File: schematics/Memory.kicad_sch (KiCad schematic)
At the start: 31 parts, among them SW1 SW_DIP_x08, U1 AS6C4008-55PCN, U2 74LS245, U3 74LS157, U4 74LS157, U5 74LS245, U6 74LS04, U7 74LS08

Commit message: chore: full part list & memory module rework
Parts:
- removed C2, C6: 0.1uF, symbol Device:C
- removed U4: 74LS157, symbol 74xx:74LS157
- removed U6: 74LS04, symbol 74xx:74LS04
- removed U7: 74LS08, symbol 74xx:74LS08
- added R9: 10K, symbol Device:R
- added SW2: SW_Push, symbol Switch:SW_Push
- added U4: 74LS00, symbol 74xx:74LS00
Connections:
- net +5V: now also U3.2 (I0a), U3.5 (I0b), R9.1, U4.14 (VCC)
- net BUS_0: now also U2.18 (B0); no longer U2.2 (A0), U5.9 (A7)
- net BUS_1: now also U2.17 (B1); no longer U2.3 (A1), U5.8 (A6)
- net BUS_2: now also U2.16 (B2); no longer U2.4 (A2), U5.7 (A5)
- net BUS_3: now also U2.15 (B3); no longer U2.5 (A3), U5.6 (A4)
- net BUS_4: now also U2.14 (B4); no longer U2.6 (A4), U5.5 (A3)
- net BUS_5: now also U2.13 (B5); no longer U2.7 (A5), U5.4 (A2)
- net BUS_6: now also U2.12 (B6); no longer U2.8 (A6), U5.3 (A1)
- net BUS_7: now also U2.11 (B7); no longer U2.9 (A7), U5.2 (A0)
- net GND: now also U5.1 (A->B), SW2.1, U4.7 (GND)
- net at D1.2 (A), U1.21 (DQ7): now also U2.9 (A7), U5.2 (A0); no longer U2.11 (B7), U3.4 (Za)
- net at D4.2 (A), U1.18 (DQ4): now also U2.6 (A4), U5.5 (A3); no longer U2.14 (B4), U3.12 (Zd)
- net at U2.1 (A->B): now also U1.29 (WE#), U3.6 (I1b), U3.9 (Zc), U4.10; no longer U5.1 (A->B)
- net at D2.2 (A), U1.20 (DQ6): now also U2.8 (A6), U5.3 (A1); no longer U2.12 (B6), U3.7 (Zb)
- net at D3.2 (A), U1.19 (DQ5): now also U2.7 (A5), U5.4 (A2); no longer U2.13 (B5), U3.9 (Zc)
- net at D5.2 (A), U1.17 (DQ3): now also U2.5 (A3), U5.6 (A4); no longer U2.15 (B3)
- net at D6.2 (A), U1.15 (DQ2): now also U2.4 (A2), U5.7 (A5); no longer U2.16 (B2)
- net at D7.2 (A), U1.14 (DQ1): now also U2.3 (A1), U5.8 (A6); no longer U2.17 (B1)
- net at D8.2 (A), U1.13 (DQ0): now also U2.2 (A0), U5.9 (A7); no longer U2.18 (B0)
- net at U2.19 (CE): now also U3.4 (Za)
- net at U5.19 (CE): now also U3.7 (Zb)
- net at SW1.10: now also U5.17 (B1)
- net at SW1.11: now also U5.16 (B2)
- net at SW1.12: now also U5.15 (B3)
- net at SW1.13: now also U5.14 (B4); no longer U3.13 (I1d)
- net at SW1.14: now also U5.13 (B5); no longer U3.10 (I1c)
- net at SW1.15: now also U5.12 (B6); no longer U3.6 (I1b)
- net at U3.3 (I1a): now also U4.6; no longer SW1.16
- net at SW1.9: now also U5.18 (B0)
- net at U3.11 (I0c): now also R9.2, SW2.2; no longer U5.16 (B2)
- net at U3.14 (I0d): no longer U5.15 (B3)
- net at U5.11 (B7): now also SW1.16
- new net: U4.4, U4.5, U4.8
- new net: U3.10 (I1c), U4.3
- new net CLK: U4.2
- new net RAM_IN: U4.1
- new net |RAM_OUT: U4.9

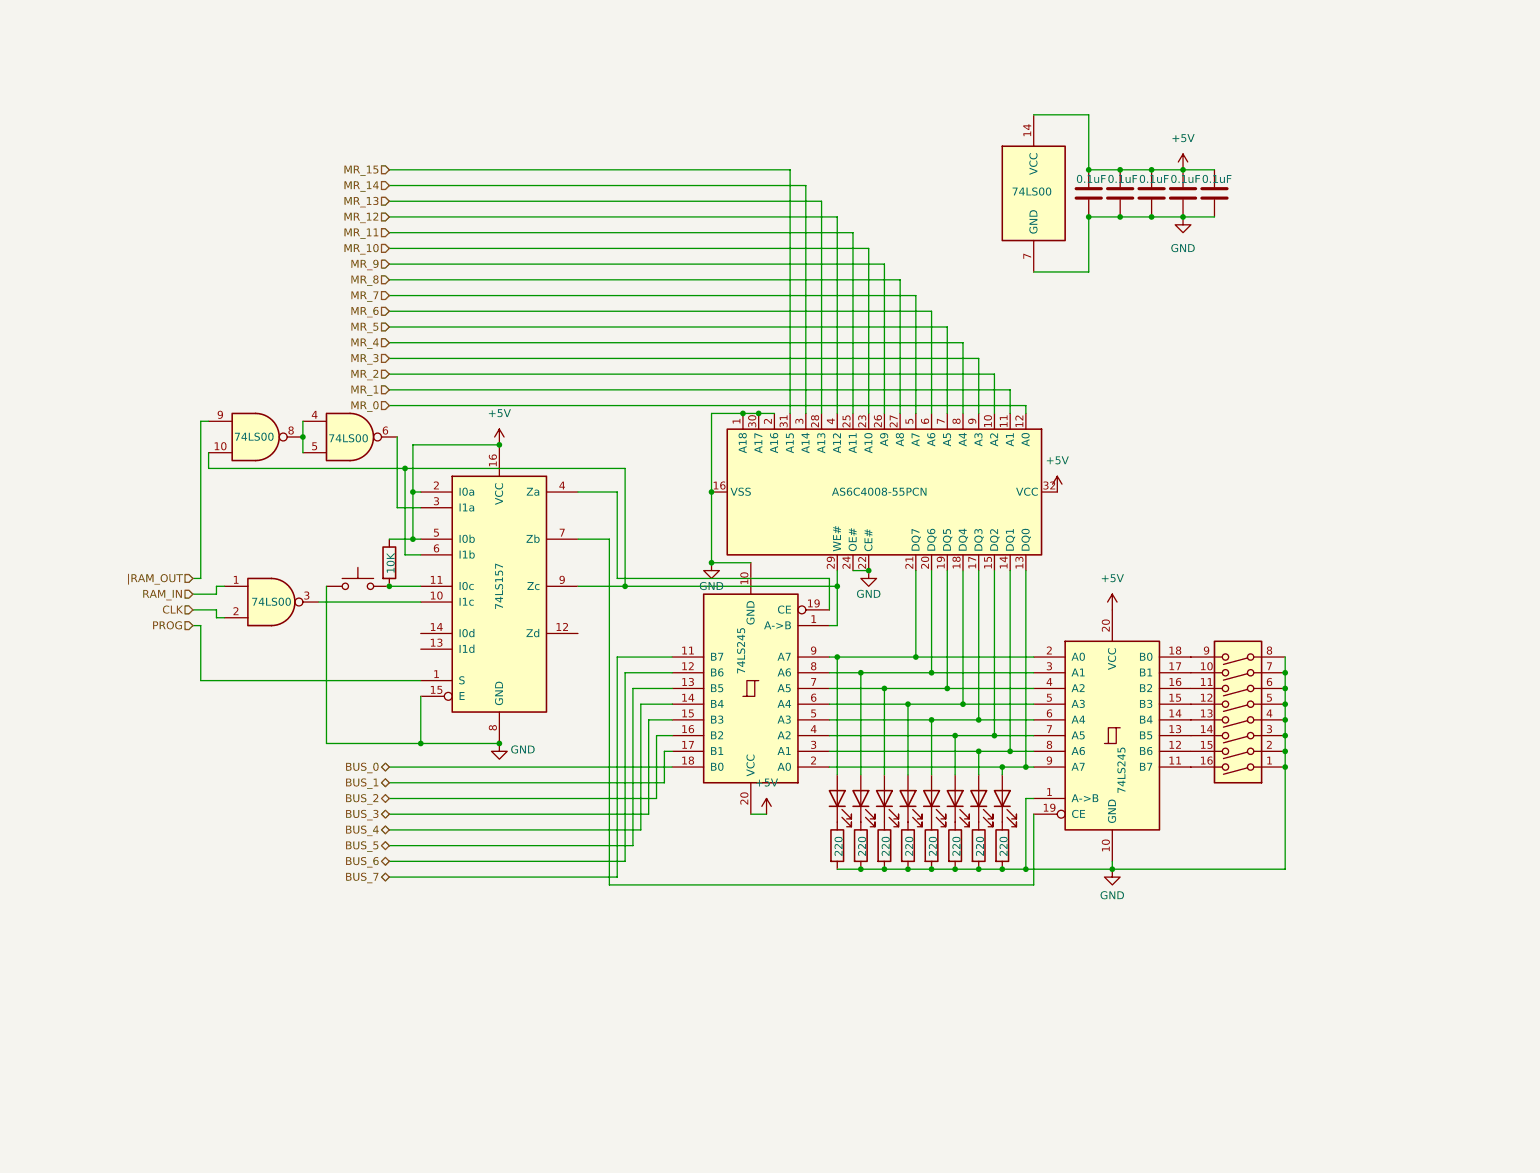
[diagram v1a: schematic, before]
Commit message: Updated schematics and README
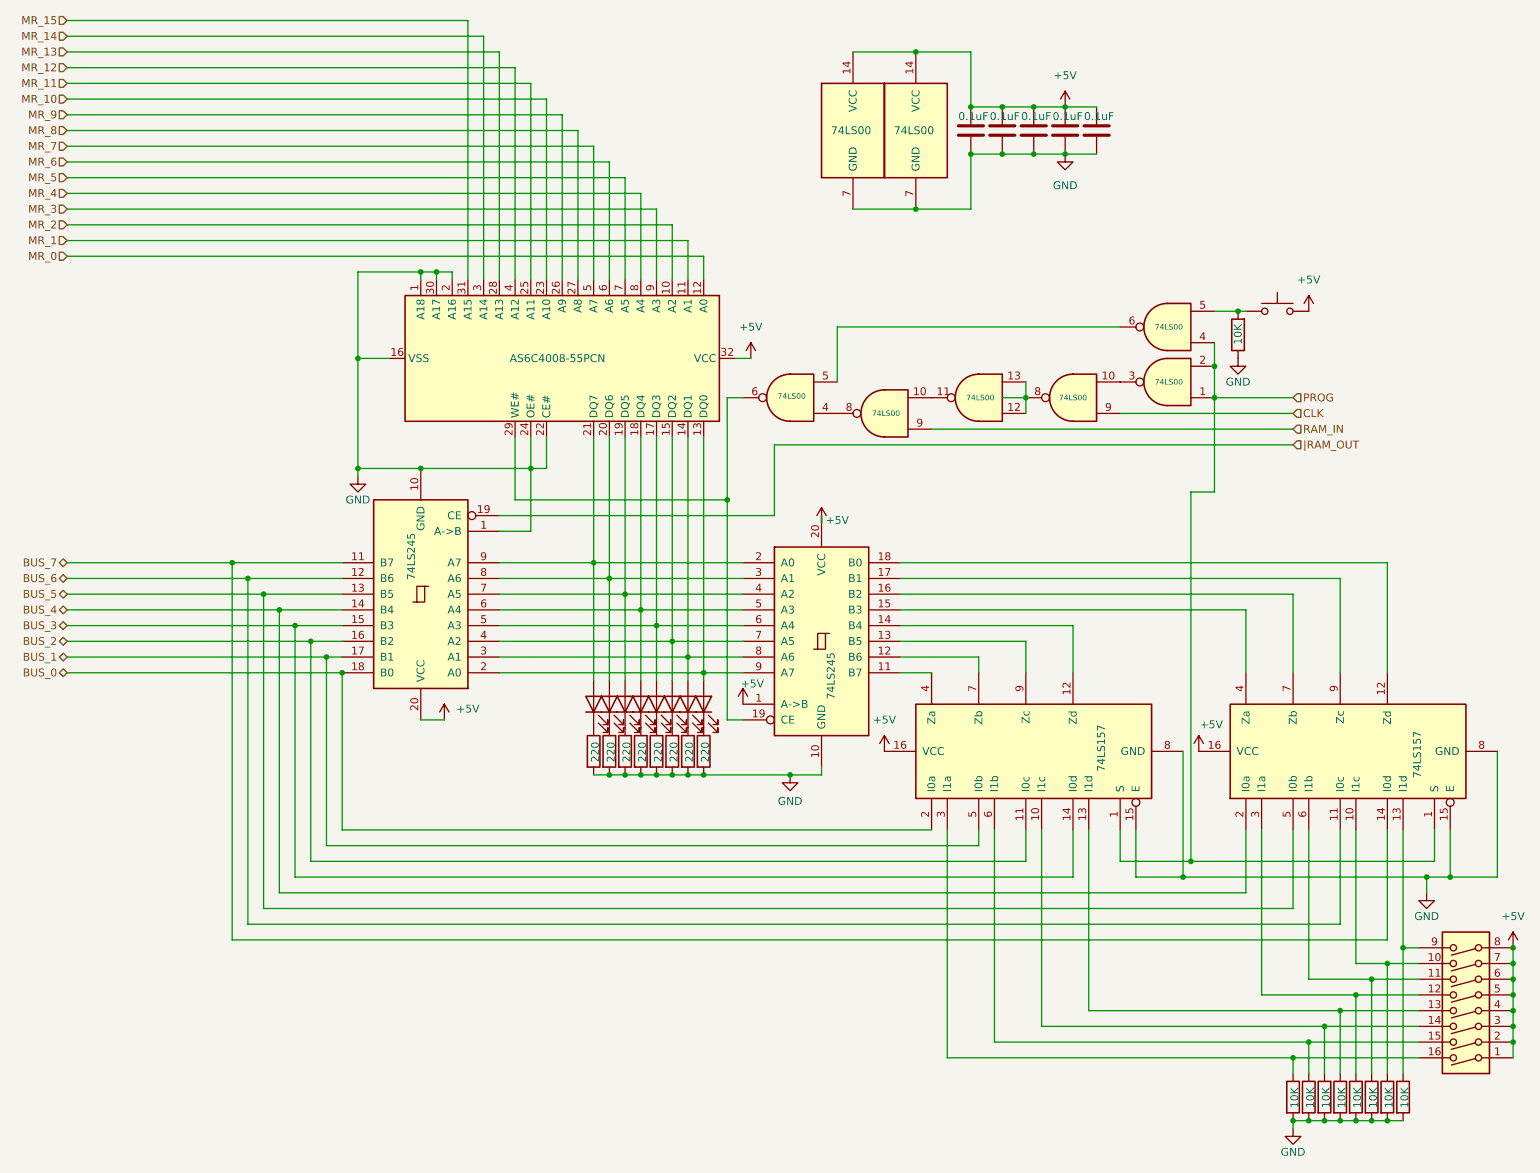
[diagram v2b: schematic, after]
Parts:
- added R10, R11, R12, R13, R14, R15, R16, R17: 10K, symbol Device:R
- added unit 4 of U4
- added U6: 74LS157, symbol 74xx:74LS157
- added U7: 74LS00, symbol 74xx:74LS00
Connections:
- net +5V: now also SW1.1, SW1.2, SW1.3, SW1.4, SW1.5, SW1.6, SW1.7, SW1.8, SW2.2, U5.1 (A->B), U6.16 (VCC), U7.14 (VCC); no longer R9.1, U3.2 (I0a), U3.5 (I0b)
- net BUS_0: now also U3.2 (I0a)
- net BUS_1: now also U3.5 (I0b)
- net BUS_2: now also U3.11 (I0c)
- net BUS_3: now also U3.14 (I0d)
- net BUS_4: now also U6.2 (I0a)
- net BUS_5: now also U6.5 (I0b)
- net BUS_6: now also U6.11 (I0c)
- net BUS_7: now also U6.14 (I0d)
- net CLK: now also U7.9; no longer U4.2
- net GND: now also R9.1, U2.1 (A->B), R10.2, R11.2, R12.2, R13.2, R14.2, R15.2, R16.2, R17.2, U6.15 (E), U6.8 (GND), U7.7 (GND); no longer SW1.1, SW1.2, SW1.3, SW1.4, SW1.5, SW1.6, SW1.7, SW1.8, SW2.1, U5.1 (A->B)
- net PROG: now also U4.1, U4.2, U4.4, U6.1 (S)
- net RAM_IN: now also U4.9; no longer U4.1
- net |RAM_OUT: now also U2.19 (CE); no longer U4.9
- net at U3.4 (Za): now also U5.11 (B7); no longer U2.19 (CE)
- net at U3.3 (I1a): now also SW1.16, R17.1; no longer U4.6
- net at SW1.10: now also R11.1, U6.10 (I1c); no longer U5.17 (B1)
- net at SW1.11: now also R12.1, U6.6 (I1b); no longer U5.16 (B2)
- net at SW1.12: now also R13.1, U6.3 (I1a); no longer U5.15 (B3)
- net at U5.14 (B4): now also U3.12 (Zd); no longer SW1.13
- net at SW1.14: now also U3.10 (I1c), R15.1; no longer U5.13 (B5)
- net at SW1.15: now also U3.6 (I1b), R16.1; no longer U5.12 (B6)
- net at SW1.9: now also R10.1, U6.13 (I1d); no longer U5.18 (B0)
- net at U4.3: now also U7.10; no longer U3.10 (I1c)
- net at U3.13 (I1d): now also SW1.13, R14.1
- net at U5.19 (CE): now also U1.29 (WE#), U7.6; no longer U3.7 (Zb)
- new net: R9.2, SW2.1, U4.5
- new net: U4.10, U4.11
- new net: U4.8, U7.4
- new net: U4.6, U7.5
- new net: U4.12, U4.13, U7.8
- new net: U3.7 (Zb), U5.12 (B6)
- new net: U3.9 (Zc), U5.13 (B5)
- new net: U5.18 (B0), U6.12 (Zd)
- new net: U5.15 (B3), U6.4 (Za)
- new net: U5.16 (B2), U6.7 (Zb)
- new net: U5.17 (B1), U6.9 (Zc)
